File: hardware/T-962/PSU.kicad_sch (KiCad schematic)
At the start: 17 parts

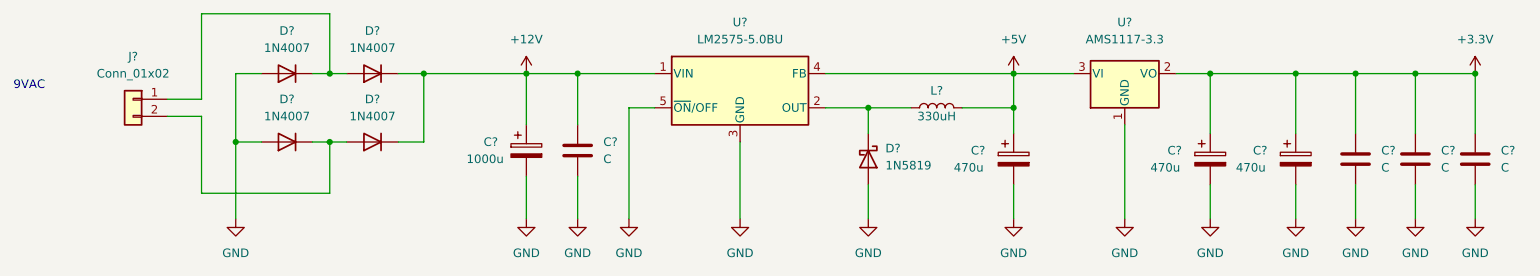
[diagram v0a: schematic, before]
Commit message: fill out designators
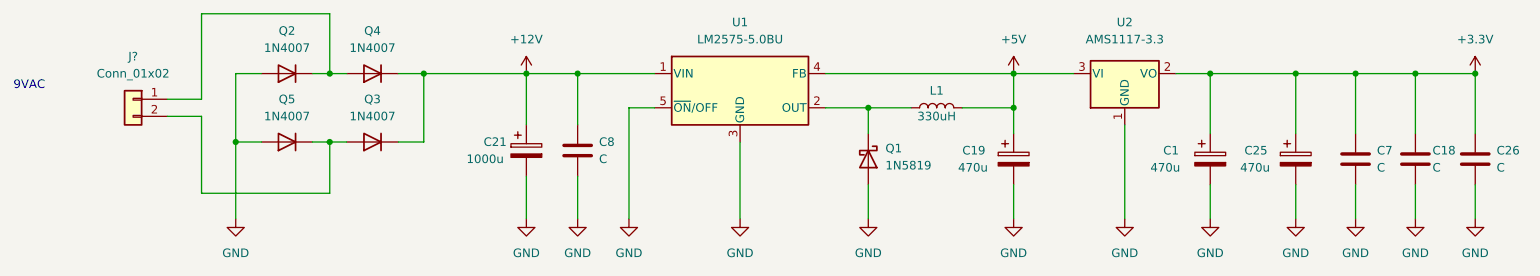
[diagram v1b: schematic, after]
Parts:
- gave numbers to parts that had none: 16
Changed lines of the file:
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@@
   (symbol (lib_id "Device:L") (at 165.1 91.44 90) (unit 1)
     (in_bom yes) (on_board yes)
-    (property "Reference" "L?" (id 0) (at 165.1 88.9 90))
+    (property "Reference" "L1" (id 0) (at 165.1 88.9 90))
     (property "Value" "330uH" (id 1) (at 165.1 92.71 90))
     (property "Footprint" "" (id 2) (at 165.1 91.44 0)
@@
   (symbol (lib_id "Diode:1N4007") (at 68.58 96.52 180) (unit 1)
     (in_bom yes) (on_board yes) (fields_autoplaced)
-    (property "Reference" "D?" (id 0) (at 68.58 90.17 0))
+    (property "Reference" "Q5" (id 0) (at 68.58 90.17 0))
     (property "Value" "1N4007" (id 1) (at 68.58 92.71 0))
     (property "Footprint" "Diode_THT:D_DO-41_SOD81_P10.16mm_Horizontal" (id 2) (at 68.58 92.075 0)
@@
   )
   (symbol (lib_id "Device:C") (at 245.11 99.06 0) (unit 1)
-    (in_bom yes) (on_board yes) (fields_autoplaced)
-    (property "Reference" "C?" (id 0) (at 248.92 97.7899 0)
-      (effects (font (size 1.27 1.27)) (justify left))
-    )
-    (property "Value" "C" (id 1) (at 248.92 100.3299 0)
+    (in_bom yes) (on_board yes)
+    (property "Reference" "C26" (id 0) (at 248.285 97.79 0)
+      (effects (font (size 1.27 1.27)) (justify left))
+    )
+    (property "Value" "C" (id 1) (at 248.285 100.33 0)
       (effects (font (size 1.27 1.27)) (justify left))
     )
@@
   (symbol (lib_id "Regulator_Switching:LM2575-5.0BU") (at 135.89 88.9 0) (unit 1)
     (in_bom yes) (on_board yes) (fields_autoplaced)
-    (property "Reference" "U?" (id 0) (at 135.89 78.74 0))
+    (property "Reference" "U1" (id 0) (at 135.89 78.74 0))
     (property "Value" "LM2575-5.0BU" (id 1) (at 135.89 81.28 0))
     (property "Footprint" "Package_TO_SOT_SMD:TO-263-5_TabPin3" (id 2) (at 135.89 95.25 0)
@@
   (symbol (lib_id "Device:C_Polarized") (at 218.44 99.06 0) (unit 1)
     (in_bom yes) (on_board yes)
-    (property "Reference" "C?" (id 0) (at 212.09 97.79 0)
-      (effects (font (size 1.27 1.27)) (justify left))
-    )
-    (property "Value" "470u" (id 1) (at 209.55 100.33 0)
+    (property "Reference" "C25" (id 0) (at 210.82 97.79 0)
+      (effects (font (size 1.27 1.27)) (justify left))
+    )
+    (property "Value" "470u" (id 1) (at 210.185 100.33 0)
       (effects (font (size 1.27 1.27)) (justify left))
     )
@@
   (symbol (lib_id "Diode:1N4007") (at 81.28 86.36 180) (unit 1)
     (in_bom yes) (on_board yes) (fields_autoplaced)
-    (property "Reference" "D?" (id 0) (at 81.28 80.01 0))
+    (property "Reference" "Q4" (id 0) (at 81.28 80.01 0))
     (property "Value" "1N4007" (id 1) (at 81.28 82.55 0))
     (property "Footprint" "Diode_THT:D_DO-41_SOD81_P10.16mm_Horizontal" (id 2) (at 81.28 81.915 0)
@@
   (symbol (lib_id "Device:C_Polarized") (at 104.14 97.79 0) (unit 1)
     (in_bom yes) (on_board yes)
-    (property "Reference" "C?" (id 0) (at 97.79 96.52 0)
+    (property "Reference" "C21" (id 0) (at 97.79 96.52 0)
       (effects (font (size 1.27 1.27)) (justify left))
     )
@@
   (symbol (lib_id "Diode:1N5819") (at 154.94 99.06 270) (unit 1)
     (in_bom yes) (on_board yes) (fields_autoplaced)
-    (property "Reference" "D?" (id 0) (at 157.48 97.4724 90)
+    (property "Reference" "Q1" (id 0) (at 157.48 97.4724 90)
       (effects (font (size 1.27 1.27)) (justify left))
     )
@@
   )
   (symbol (lib_id "Device:C") (at 227.33 99.06 0) (unit 1)
-    (in_bom yes) (on_board yes) (fields_autoplaced)
-    (property "Reference" "C?" (id 0) (at 231.14 97.7899 0)
-      (effects (font (size 1.27 1.27)) (justify left))
-    )
-    (property "Value" "C" (id 1) (at 231.14 100.3299 0)
+    (in_bom yes) (on_board yes)
+    (property "Reference" "C7" (id 0) (at 230.505 97.79 0)
+      (effects (font (size 1.27 1.27)) (justify left))
+    )
+    (property "Value" "C" (id 1) (at 230.505 100.33 0)
       (effects (font (size 1.27 1.27)) (justify left))
     )
@@
   (symbol (lib_id "Device:C_Polarized") (at 205.74 99.06 0) (unit 1)
     (in_bom yes) (on_board yes)
-    (property "Reference" "C?" (id 0) (at 199.39 97.79 0)
+    (property "Reference" "C1" (id 0) (at 198.755 97.79 0)
       (effects (font (size 1.27 1.27)) (justify left))
     )
@@
   (symbol (lib_id "Regulator_Linear:AMS1117-3.3") (at 193.04 86.36 0) (unit 1)
     (in_bom yes) (on_board yes) (fields_autoplaced)
-    (property "Reference" "U?" (id 0) (at 193.04 78.74 0))
+    (property "Reference" "U2" (id 0) (at 193.04 78.74 0))
     (property "Value" "AMS1117-3.3" (id 1) (at 193.04 81.28 0))
     (property "Footprint" "Package_TO_SOT_SMD:SOT-223-3_TabPin2" (id 2) (at 193.04 81.28 0)
@@
   (symbol (lib_id "Device:C_Polarized") (at 176.53 99.06 0) (unit 1)
     (in_bom yes) (on_board yes)
-    (property "Reference" "C?" (id 0) (at 170.18 97.79 0)
-      (effects (font (size 1.27 1.27)) (justify left))
-    )
-    (property "Value" "470u" (id 1) (at 167.64 100.33 0)
+    (property "Reference" "C19" (id 0) (at 168.91 97.79 0)
+      (effects (font (size 1.27 1.27)) (justify left))
+    )
+    (property "Value" "470u" (id 1) (at 168.275 100.33 0)
       (effects (font (size 1.27 1.27)) (justify left))
     )
@@
   )
   (symbol (lib_id "Device:C") (at 236.22 99.06 0) (unit 1)
-    (in_bom yes) (on_board yes) (fields_autoplaced)
-    (property "Reference" "C?" (id 0) (at 240.03 97.7899 0)
-      (effects (font (size 1.27 1.27)) (justify left))
-    )
-    (property "Value" "C" (id 1) (at 240.03 100.3299 0)
+    (in_bom yes) (on_board yes)
+    (property "Reference" "C18" (id 0) (at 238.76 97.79 0)
+      (effects (font (size 1.27 1.27)) (justify left))
+    )
+    (property "Value" "C" (id 1) (at 238.76 100.33 0)
       (effects (font (size 1.27 1.27)) (justify left))
     )
@@
   (symbol (lib_id "Diode:1N4007") (at 81.28 96.52 180) (unit 1)
     (in_bom yes) (on_board yes) (fields_autoplaced)
-    (property "Reference" "D?" (id 0) (at 81.28 90.17 0))
+    (property "Reference" "Q3" (id 0) (at 81.28 90.17 0))
     (property "Value" "1N4007" (id 1) (at 81.28 92.71 0))
     (property "Footprint" "Diode_THT:D_DO-41_SOD81_P10.16mm_Horizontal" (id 2) (at 81.28 92.075 0)
@@
   )
   (symbol (lib_id "Device:C") (at 111.76 97.79 0) (unit 1)
-    (in_bom yes) (on_board yes) (fields_autoplaced)
-    (property "Reference" "C?" (id 0) (at 115.57 96.5199 0)
-      (effects (font (size 1.27 1.27)) (justify left))
-    )
-    (property "Value" "C" (id 1) (at 115.57 99.0599 0)
+    (in_bom yes) (on_board yes)
+    (property "Reference" "C8" (id 0) (at 114.935 96.52 0)
+      (effects (font (size 1.27 1.27)) (justify left))
+    )
+    (property "Value" "C" (id 1) (at 114.935 99.06 0)
       (effects (font (size 1.27 1.27)) (justify left))
     )
@@
   (symbol (lib_id "Diode:1N4007") (at 68.58 86.36 180) (unit 1)
     (in_bom yes) (on_board yes) (fields_autoplaced)
-    (property "Reference" "D?" (id 0) (at 68.58 80.01 0))
+    (property "Reference" "Q2" (id 0) (at 68.58 80.01 0))
     (property "Value" "1N4007" (id 1) (at 68.58 82.55 0))
     (property "Footprint" "Diode_THT:D_DO-41_SOD81_P10.16mm_Horizontal" (id 2) (at 68.58 81.915 0)
